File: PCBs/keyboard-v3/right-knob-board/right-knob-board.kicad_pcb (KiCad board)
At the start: 2 copper layers, 58 x 58 mm, 7 parts

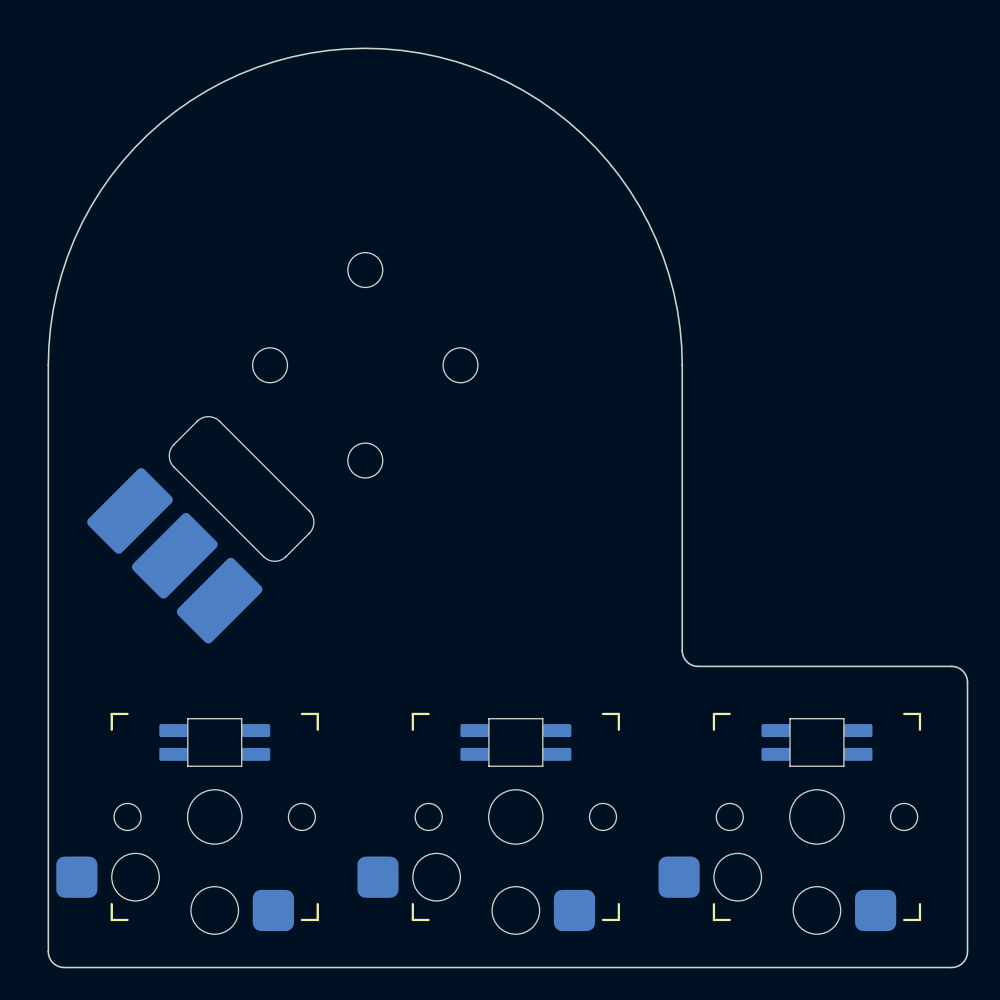
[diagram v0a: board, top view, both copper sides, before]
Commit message: Right control board schematic almost done
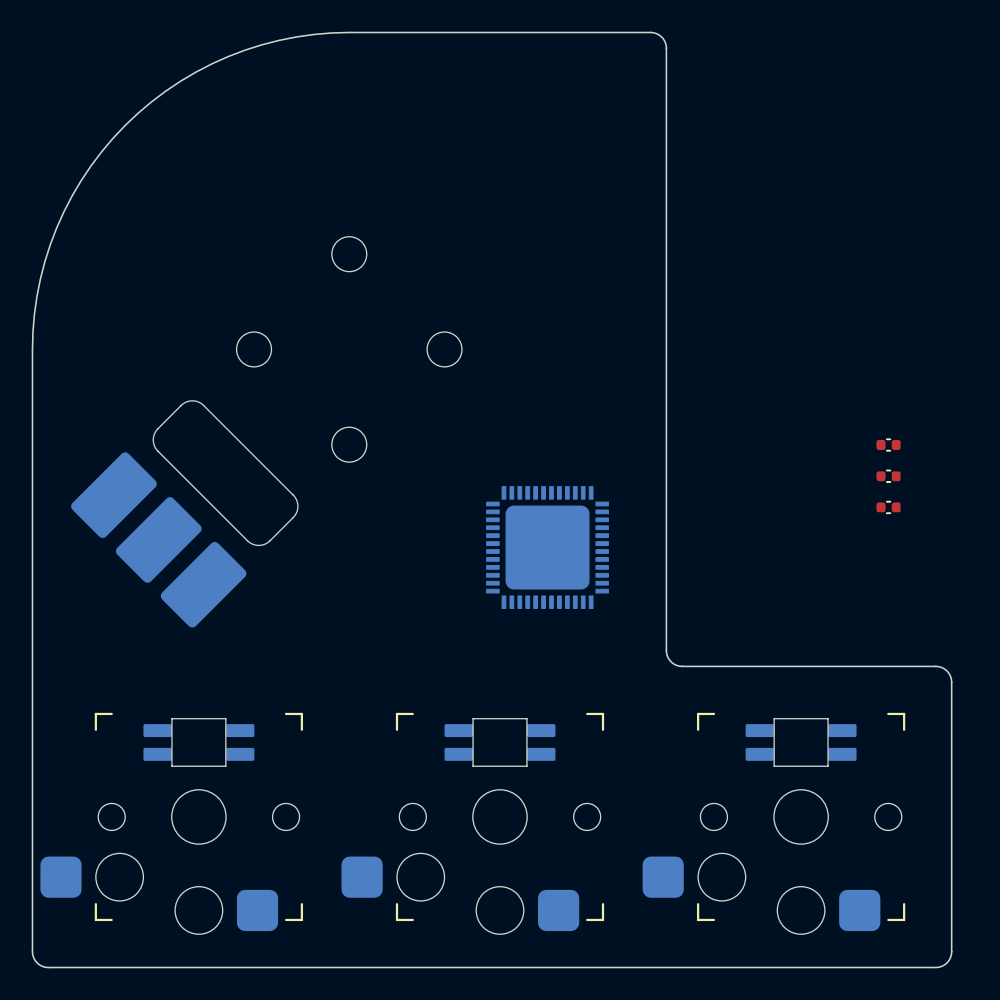
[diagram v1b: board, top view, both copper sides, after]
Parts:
- removed REF**: 2206-100T, project_footprints:2206-100T
- removed REF** (x2): SW_Kailh_Choc_V1_HotSwap, project_footprints:SW_Kailh_Choc_V1_HotSwap
- added C1: 1u, project_footprints:C_0402, F.Cu at (172.0, 86.0)
- added C2: 100n, project_footprints:C_0402, F.Cu at (172.0, 88.0)
- added C3: 4u7, project_footprints:C_0402, F.Cu at (172.0, 90.0)
- added M1: 2206-100T, project_footprints:2206-100T, F.Cu at (138.0, 80.0)
- added SW2: SW_DIP_x01, project_footprints:SW_Kailh_Choc_V1_HotSwap, F.Cu at (147.5, 109.5)
- added SW3: SW_DIP_x01, project_footprints:SW_Kailh_Choc_V1_HotSwap, F.Cu at (166.5, 109.5)
- added U1: STM32G0C1CEUx, project_footprints:QFN50P700X700X60-49N-D, B.Cu at (150.5, 92.5)
- D1, D2, D3: renamed from REF**; value ${REFERENCE} -> SK6812-E
- SW1: renamed from REF**; value SW_Kailh_Choc_V1_HotSwap -> SW_DIP_x01
- moved D1 1.00 mm to (128.5, 104.8)
- moved D2 1.00 mm to (147.5, 104.8)
- moved D3 1.00 mm to (166.5, 104.8)
- moved SW1 1.00 mm to (128.5, 109.5)
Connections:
- D1 pad 1: (no net) -> VBUS
- D1 pad 2: (no net) -> /LED2
- D1 pad 3: (no net) -> GND
- D1 pad 4: (no net) -> /LED1
- D2 pad 1: (no net) -> VBUS
- D2 pad 2: (no net) -> /LED3
- D2 pad 3: (no net) -> GND
- D2 pad 4: (no net) -> /LED2
- D3 pad 1: (no net) -> VBUS
- D3 pad 2: (no net) -> unconnected-(D3-DOUT-Pad2)
- D3 pad 3: (no net) -> GND
- D3 pad 4: (no net) -> /LED3
- SW1 pad 1: (no net) -> GND
- SW1 pad 2: (no net) -> /KEY_T4
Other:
- board size 58 x 58 mm -> 58 x 59 mm

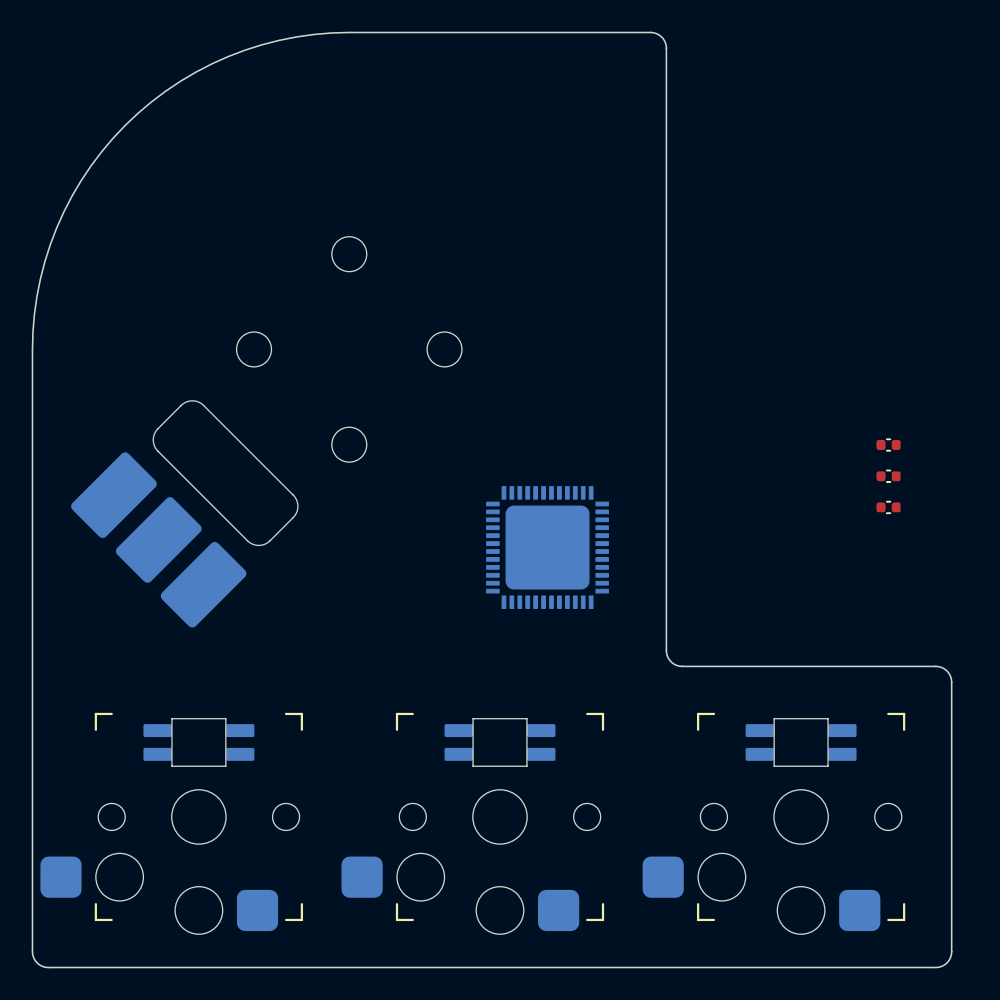
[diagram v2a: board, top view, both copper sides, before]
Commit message: Right daughter boards finished
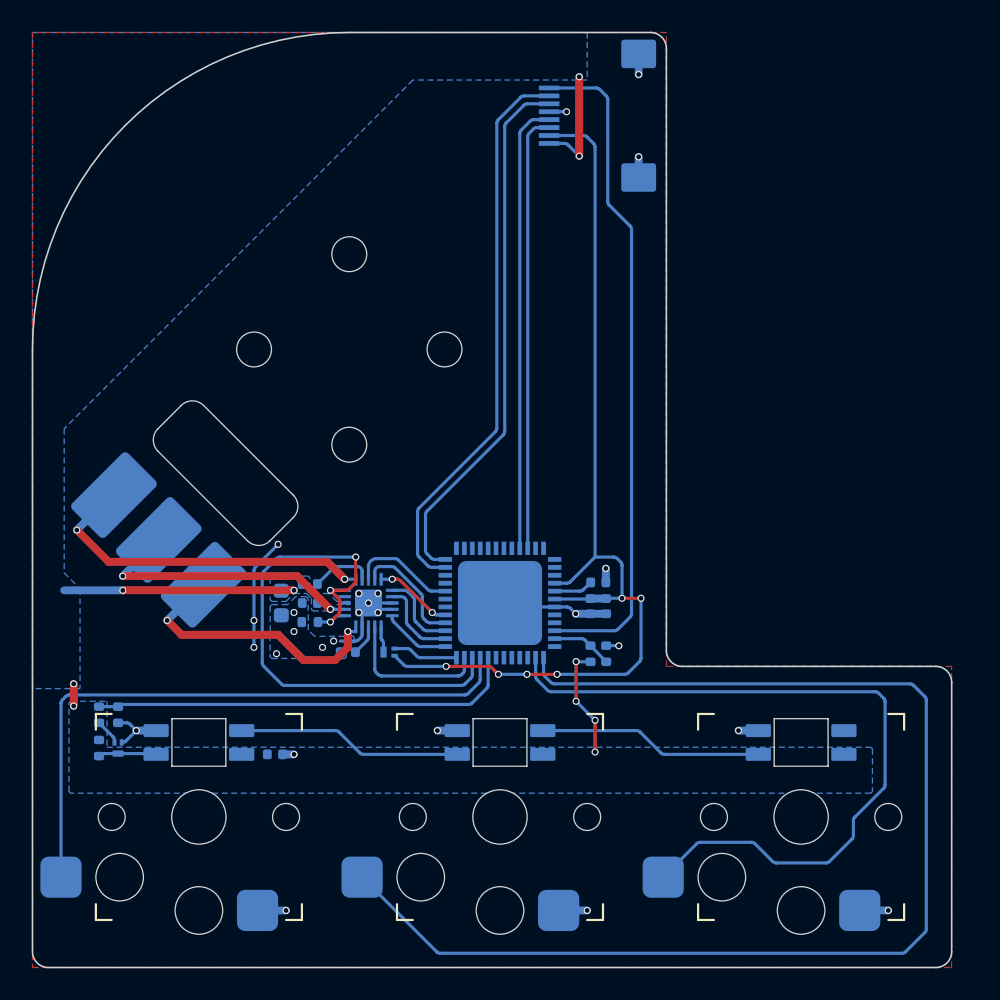
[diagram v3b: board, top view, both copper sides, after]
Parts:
- added C101: 100n, project_footprints:C_0402, B.Cu at (135.5, 94.8)
- added C102: 100n, project_footprints:C_0402, B.Cu at (135.5, 96.0)
- added C103: 22u, project_footprints:C_0603, B.Cu at (133.7, 96.0)
- added C104: 100n, project_footprints:C_0402, B.Cu at (137.9, 99.1)
- added C201: 1u, project_footprints:C_0402, B.Cu at (133.3, 105.5)
- added J101: F31L-1A7H1-11008, project_footprints:F31L-1A7H1-11008, B.Cu at (154.1, 65.2)
- added Q101: DMP21D0UFB-7B, project_footprints:DMP21D0UFB7B, B.Cu at (140.5, 99.1)
- added Q201: DMN21D2UFB-7B, project_footprints:DMN21D2UFB7B, B.Cu at (123.4, 105.2)
- added R101: 1R, project_footprints:R_0402, B.Cu at (135.5, 97.2)
- added R102: 10k, project_footprints:R_0402, B.Cu at (153.2, 99.2)
- added R103: 2k2, project_footprints:R_0402, B.Cu at (154.2, 99.2)
- added R201: 2k2, project_footprints:R_0402, B.Cu at (122.2, 105.2)
- added R202: 2k2, project_footprints:R_0402, B.Cu at (122.2, 103.0)
- added R203: 10k, project_footprints:R_0402, B.Cu at (123.4, 103.0)
- added U101: TMC6300-LA, project_footprints:QFN40P300X300X90-21N, B.Cu at (139.2, 96.0)
- C1, C2, C3: moved to B.Cu
- moved C2 20.5 mm to (153.2, 96.2), turned to -90 degrees
- moved C1 20.3 mm to (153.7, 94.7)
- moved C3 18.9 mm to (154.2, 96.2), turned to -90 degrees
- moved U1 4.61 mm to (147.5, 96.0), turned to 180 degrees
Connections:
- net VBUS renamed +5V
- M1 pad 1: unconnected-(M1-A-Pad1) -> /U
- M1 pad 2: unconnected-(M1-B-Pad2) -> /V
- M1 pad 3: unconnected-(M1-C-Pad3) -> /W
- SW1 pad 2: /KEY_T4 -> /KEY_G5
- SW2 pad 2: /KEY_T5 -> /KEY_H5
- SW3 pad 2: /KEY_T6 -> /KEY_I5
- U1 pad 11: unconnected-(U1-PA0-Pad11) -> /5V_SENSE
- U1 pad 13: unconnected-(U1-PA2-Pad13) -> /KEY_H5
- U1 pad 14: unconnected-(U1-PA3-Pad14) -> /KEY_I5
- U1 pad 20: unconnected-(U1-PB1-Pad20) -> /NEOPIXEL
- U1 pad 21: unconnected-(U1-PB2-Pad21) -> /KEY_G5
- U1 pad 22: unconnected-(U1-PB10-Pad22) -> /ISENSE
- U1 pad 23: unconnected-(U1-PB11-Pad23) -> /DIAG
- U1 pad 24: unconnected-(U1-PB12-Pad24) -> /STANDBY
- U1 pad 25: unconnected-(U1-PB13-Pad25) -> /VL
- U1 pad 26: unconnected-(U1-PB14-Pad26) -> /WL
- U1 pad 27: unconnected-(U1-PB15-Pad27) -> /UL
- U1 pad 28: unconnected-(U1-PA8-Pad28) -> /VH
- U1 pad 29: unconnected-(U1-PA9/UCPD1_DBCC1-Pad29) -> /WH
- U1 pad 32: unconnected-(U1-PA10/UCPD1_DBCC2-Pad32) -> /UH
- U1 pad 33: /DN -> unconnected-(U1-PA9/PA11-Pad33)
- U1 pad 34: /DP -> unconnected-(U1-PA10/PA12-Pad34)
- U1 pad 45: unconnected-(U1-PB6-Pad45) -> /RX
- U1 pad 46: unconnected-(U1-PB7-Pad46) -> /TX
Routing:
- net /KEY_H5: track 0.00 -> 78.6 mm
- net +3V3: track 0.00 -> 62.1 mm, vias 0 -> 6
- net /KEY_I5: track 0.00 -> 47.4 mm
- net /~{RST}: track 0.00 -> 42.4 mm
- net /KEY_G5: track 0.00 -> 39.5 mm
- net GND: track 0.00 -> 38.8 mm, vias 0 -> 26
- net /ISENSE: track 0.00 -> 35.8 mm, vias 0 -> 3
- net /SWDIO: track 0.00 -> 35.4 mm
- net /SWCLK: track 0.00 -> 33.8 mm
- net +5V: track 0.00 -> 30.2 mm, vias 0 -> 10
- net /RX: track 0.00 -> 28.4 mm
- net /TX: track 0.00 -> 27.6 mm
- net /NEOPIXEL: track 0.00 -> 26.9 mm
- net /W: track 0.00 -> 22.1 mm, vias 0 -> 2
- net /V: track 0.00 -> 18.1 mm, vias 0 -> 2
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- added copper zone on B.Cu, net +5V
- added copper zone on B.Cu, net GND
- added copper zone on F.Cu, net GND

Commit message: Added debug-breakout board, progress on right side schematics & layout
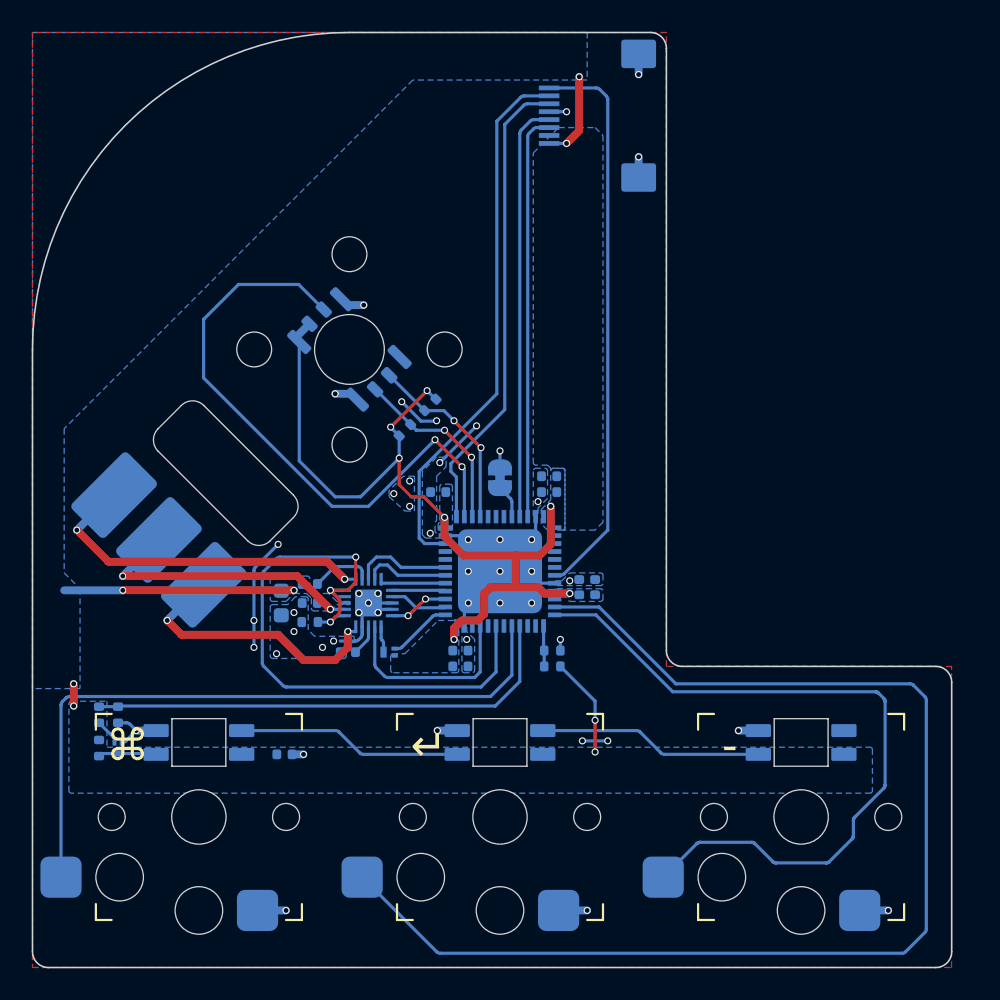
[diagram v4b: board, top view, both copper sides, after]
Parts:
- removed R102: 10k, project_footprints:R_0402
- removed R103: 2k2, project_footprints:R_0402
- removed U1: STM32G0C1CEUx, project_footprints:QFN50P700X700X60-49N-D
- added C105: 4u7, project_footprints:C_0402, B.Cu at (150.6, 88.0)
- added C106: 100n, project_footprints:C_0402, B.Cu at (150.6, 89.0)
- added C107: 100n, project_footprints:C_0402, B.Cu at (143.6, 89.0)
- added C108: 100n, project_footprints:C_0402, B.Cu at (152.5, 95.0)
- added JP101: SolderJumper_2_Bridged, Jumper:SolderJumper-2_P1.3mm_Bridged_RoundedPad1.0x1.5mm, B.Cu at (147.5, 88.1)
- added R104: 10k, project_footprints:R_0402, B.Cu at (143.1, 83.5)
- added R105: 10k, project_footprints:R_0402, B.Cu at (141.5, 85.1)
- added R106: 10k, project_footprints:R_0402, B.Cu at (150.8, 100.0)
- added R107: 2k2, project_footprints:R_0402, B.Cu at (150.8, 99.0)
- added U102: AS5600, project_footprints:as5600-rear-magnet, B.Cu at (138.0, 80.0)
- added U103: STM32U031C6Ux, project_footprints:QFN50P700X700X60-49N-D, B.Cu at (147.5, 94.0)
- moved C3 9.62 mm to (145.0, 99.0), turned to 0 degrees
- moved C2 9.04 mm to (145.0, 100.0), turned to 0 degrees
- moved C201 0.60 mm to (133.9, 105.5)
- moved C1 0.36 mm to (153.5, 95.0), turned to 90 degrees
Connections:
- C1 pad 1: /VREF+ -> +3V3
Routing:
- net /ANGLE: track 0.00 -> 38.2 mm, vias 0 -> 2
- net GND: track 38.8 -> 59.4 mm, vias 26 -> 49
- net /SDA: track 0.00 -> 12.1 mm, vias 0 -> 2
- net /SCL: track 0.00 -> 11.6 mm, vias 0 -> 2
- net +3V3: track 62.1 -> 51.7 mm, vias 6 -> 7
- net /~{RST}: track 42.4 -> 35.7 mm
- net /SWCLK: track 33.8 -> 29.6 mm
- net /NEOPIXEL: track 26.9 -> 30.7 mm
- net /KEY_G5: track 39.5 -> 43.2 mm
- net /ISENSE: track 35.8 -> 39.3 mm
- net /DIAG: track 9.52 -> 12.5 mm
- net /VREF+: track 2.48 -> 0.00 mm
- net +5V: track 30.2 -> 27.8 mm, vias 10 -> 8
- net /BOOT0: track 0.00 -> 2.10 mm
- net /TX: track 27.6 -> 25.6 mm
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- added copper zone on B.Cu, net +3V3
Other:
- board text added: "-"
- board text added: "↵"
- board text added: "⌘"

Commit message: Added power gate to AS5600 to reduce its sleep current
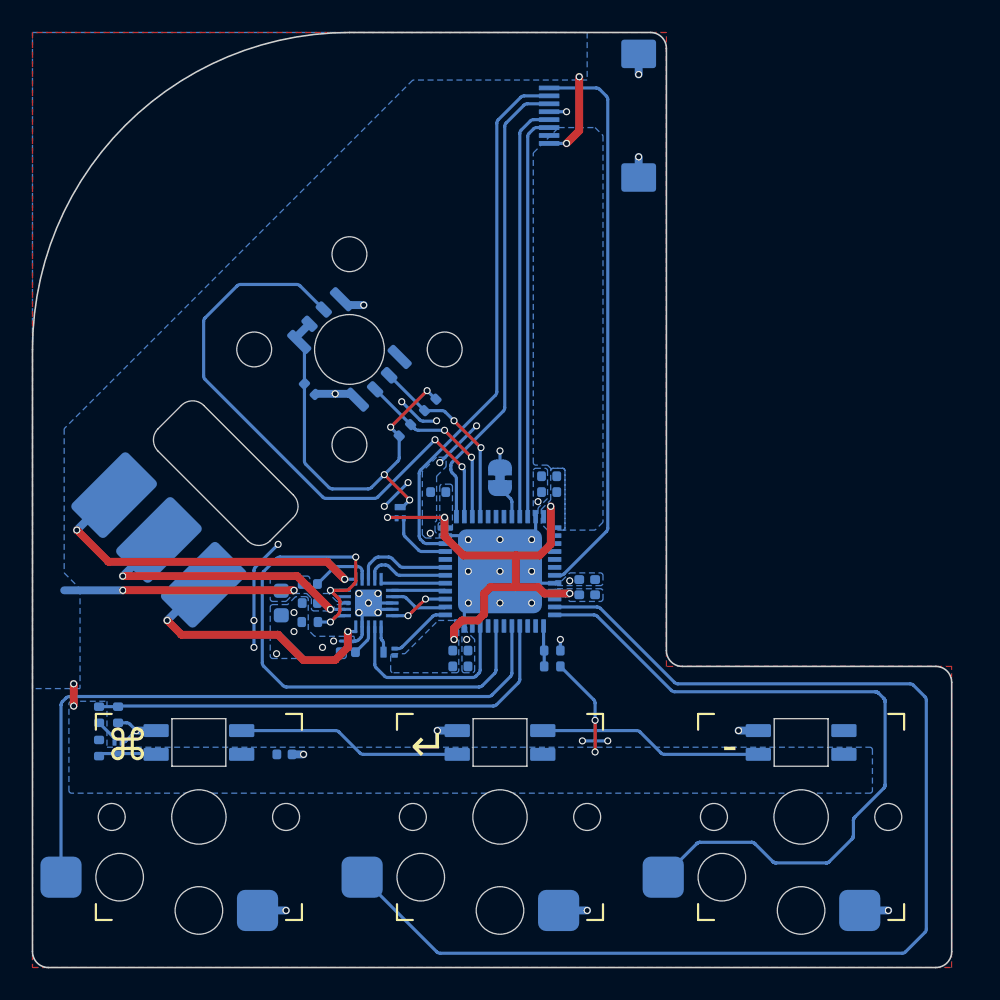
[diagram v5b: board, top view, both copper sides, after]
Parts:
- added C109: 100n, project_footprints:C_0402, B.Cu at (135.5, 82.5)
- added Q102: DMP21D0UFB-7B, project_footprints:DMP21D0UFB7B, B.Cu at (141.2, 90.3)
- R101: value 1R -> 500m
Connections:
- R104 pad 1: +3V3 -> /ENC_3V3
- R105 pad 1: +3V3 -> /ENC_3V3
- U102 pad 1: +3V3 -> /ENC_3V3
- U102 pad 2: +3V3 -> /ENC_3V3
- U103 pad 33: unconnected-(U103-PA12-Pad33) -> /~{ENC_EN}
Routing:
- net /ENC_3V3: track 0.00 -> 25.7 mm, vias 0 -> 4
- net +3V3: track 51.7 -> 27.3 mm, vias 7 -> 5
- net /~{ENC_EN}: track 0.00 -> 4.10 mm
- net GND: track 59.4 -> 62.7 mm, vias 49 -> 48
- net /ANGLE: track 38.2 -> 37.6 mm

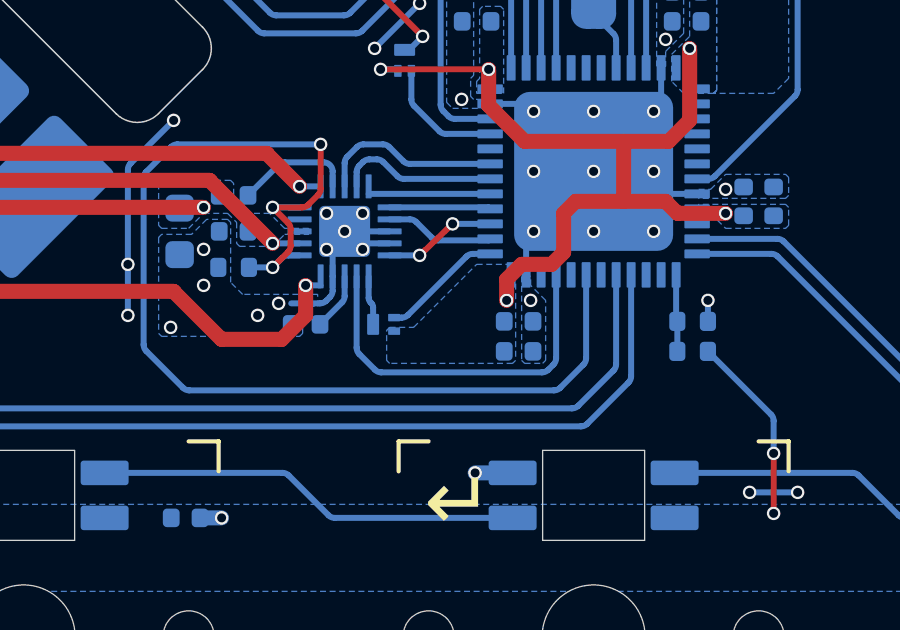
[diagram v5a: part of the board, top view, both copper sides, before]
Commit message: Right control board placement and schematic done
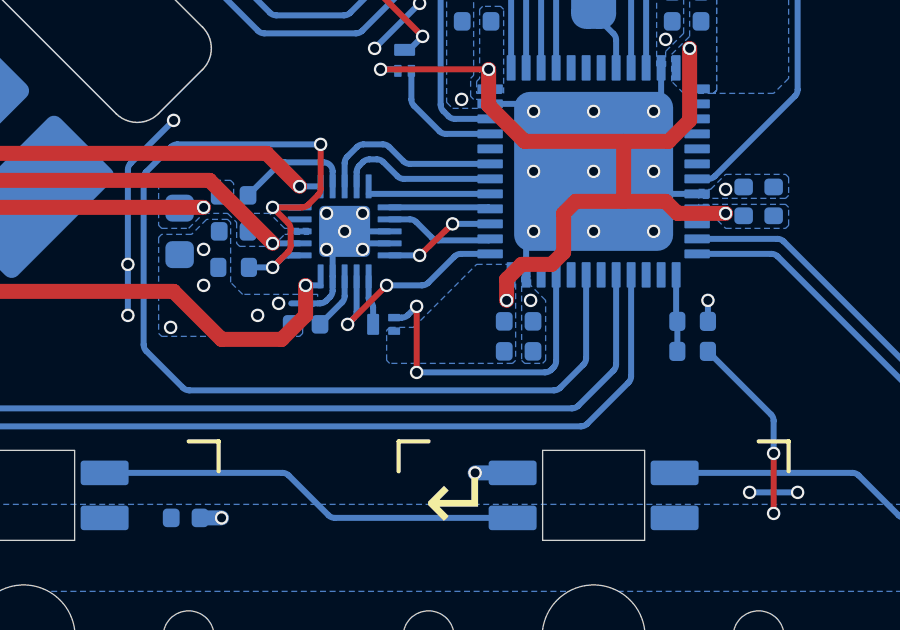
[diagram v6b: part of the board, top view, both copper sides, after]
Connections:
- U103 pad 21: /DIAG -> /STANDBY
- U103 pad 25: /STANDBY -> /DIAG
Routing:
- net /STANDBY: track 4.05 -> 10.8 mm, vias 0 -> 2
- net /DIAG: track 12.4 -> 7.40 mm, vias 0 -> 2
